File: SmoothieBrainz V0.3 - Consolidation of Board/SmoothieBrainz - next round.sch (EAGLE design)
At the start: 156 parts, among them IC1 LPC1769, IC5 LD117ADT33TR, Q1 BSL207SP, Q2 12MHz, SW1 SW_TACT_4P_B, SW3 SW_TACT_4P_B, U2 HC_05, U3 USD-SOCKETUSD, X1 GMSTBV2, X14 USBPTH, X2 MSTBA2, X3 MSTBA4

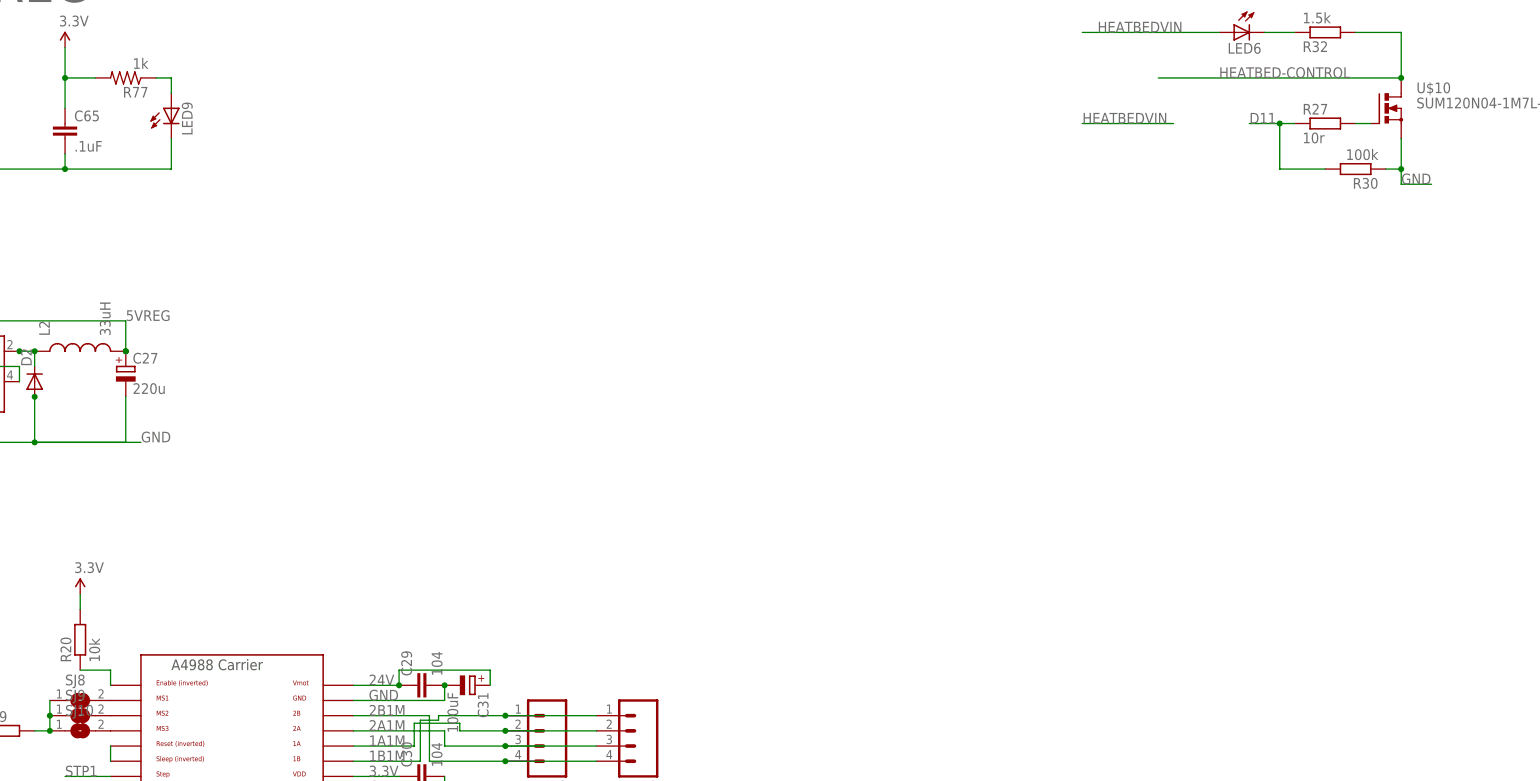
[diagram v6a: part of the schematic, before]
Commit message: lan8720 routed, added mosfets
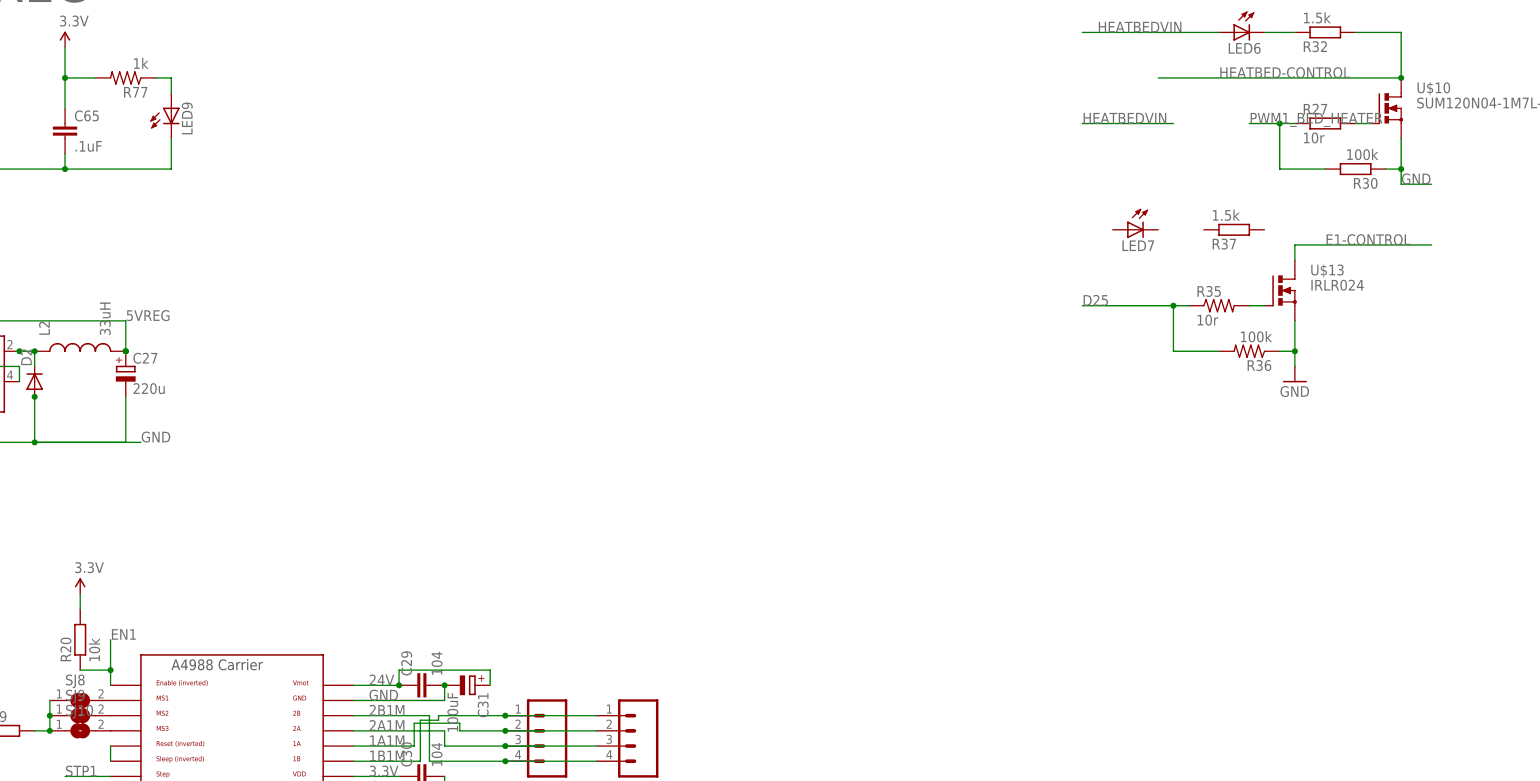
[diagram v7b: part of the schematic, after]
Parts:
- added LED7: (no value), led:LEDSML0805
- added R35: 10r, adafruit:R-US_R0805
- added R36: 100k, adafruit:R-US_R0805
- added R37: 1.5k, resistor:R-EU_R0603
- added U$13: IRLR024, Cohesion_parts:N-POWER-MOSFETDPAK-MOSFET
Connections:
- removed net D11: R27.1, R30.2
- new net D25: R35.1, R36.2
- new net E1-CONTROL: U$13.D
- net EN1: now also R20.1, U$1.EN
- net GND: now also R36.1, U$13.S
- net N$28: now also R35.2, U$13.G; no longer R20.1, U$1.EN
- net PWM1_BED_HEATER: now also R27.1, R30.2
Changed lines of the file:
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@@
 <class number="4" name="30-Amp Class" width="2.54" drill="0">
 </class>
+<class number="5" name="3.3-Amp Class" width="1.27" drill="0">
+</class>
 </classes>
 <parts>
@@
 <part name="U$11" library="adafruit" deviceset="FIDUCIAL" device=""/>
 <part name="U$12" library="adafruit" deviceset="FIDUCIAL" device=""/>
+<part name="U$13" library="Cohesion_parts" deviceset="N-POWER-MOSFET" device="DPAK-MOSFET" value="IRLR024"/>
+<part name="R35" library="adafruit" deviceset="R-US_" device="R0805" value="10r"/>
+<part name="R36" library="adafruit" deviceset="R-US_" device="R0805" value="100k"/>
+<part name="GND15" library="supply1" deviceset="GND" device=""/>
+<part name="LED7" library="led" deviceset="LED" device="SML0805"/>
+<part name="R37" library="resistor" deviceset="R-EU_" device="R0603" value="1.5k"/>
 </parts>
 <sheets>
@@
 <instance part="U$11" gate="G$1" x="17.78" y="215.9"/>
 <instance part="U$12" gate="G$1" x="27.94" y="215.9"/>
+<instance part="U$13" gate="G$1" x="528.32" y="335.28"/>
+<instance part="R35" gate="G$1" x="508" y="332.74"/>
+<instance part="R36" gate="G$1" x="513.08" y="325.12" rot="R180"/>
+<instance part="GND15" gate="1" x="520.7" y="320.04"/>
+<instance part="LED7" gate="G$1" x="492.76" y="345.44" rot="MR270"/>
+<instance part="R37" gate="G$1" x="510.54" y="345.44" rot="MR180"/>
 </instances>
 <busses>
@@
 <label x="78.74" y="281.94" size="1.778" layer="95"/>
 </segment>
+<segment>
+<pinref part="R36" gate="G$1" pin="1"/>
+<pinref part="U$13" gate="G$1" pin="S"/>
+<wire x1="518.16" y1="325.12" x2="520.7" y2="325.12" width="0.1524" layer="91"/>
+<wire x1="520.7" y1="325.12" x2="520.7" y2="330.2" width="0.1524" layer="91"/>
+<pinref part="GND15" gate="1" pin="GND"/>
+<wire x1="520.7" y1="322.58" x2="520.7" y2="325.12" width="0.1524" layer="91"/>
+<junction x="520.7" y="325.12"/>
+</segment>
 </net>
 <net name="3.3V" class="0">
@@
 <wire x1="78.74" y1="398.78" x2="106.68" y2="398.78" width="0.1524" layer="91"/>
 </segment>
+<segment>
+<pinref part="U$1" gate="G$1" pin="EN"/>
+<wire x1="322.58" y1="269.24" x2="322.58" y2="271.78" width="0.1524" layer="91"/>
+<pinref part="R20" gate="G$1" pin="1"/>
+<wire x1="317.5" y1="271.78" x2="322.58" y2="271.78" width="0.1524" layer="91"/>
+<wire x1="322.58" y1="271.78" x2="322.58" y2="276.86" width="0.1524" layer="91"/>
+<junction x="322.58" y="271.78"/>
+<label x="322.58" y="276.86" size="1.778" layer="95"/>
+</segment>
 </net>
 <net name="DIR1" class="0">
@@
 <wire x1="78.74" y1="444.5" x2="106.68" y2="444.5" width="0.1524" layer="91"/>
 </segment>
+<segment>
+<pinref part="R30" gate="G$1" pin="2"/>
+<wire x1="525.78" y1="355.6" x2="518.16" y2="355.6" width="0.1524" layer="91"/>
+<wire x1="518.16" y1="355.6" x2="518.16" y2="363.22" width="0.1524" layer="91"/>
+<pinref part="R27" gate="G$1" pin="1"/>
+<wire x1="518.16" y1="363.22" x2="520.7" y2="363.22" width="0.1524" layer="91"/>
+<wire x1="518.16" y1="363.22" x2="513.08" y2="363.22" width="0.1524" layer="91"/>
+<junction x="518.16" y="363.22"/>
+<label x="513.08" y="363.22" size="1.778" layer="95"/>
+</segment>
 </net>
 <net name="Y_MIN" class="0">
@@
 </segment>
 </net>
-<net name="D11" class="0">
-<segment>
-<pinref part="R30" gate="G$1" pin="2"/>
-<wire x1="525.78" y1="355.6" x2="518.16" y2="355.6" width="0.1524" layer="91"/>
-<wire x1="518.16" y1="355.6" x2="518.16" y2="363.22" width="0.1524" layer="91"/>
-<pinref part="R27" gate="G$1" pin="1"/>
-<wire x1="518.16" y1="363.22" x2="520.7" y2="363.22" width="0.1524" layer="91"/>
-<wire x1="518.16" y1="363.22" x2="513.08" y2="363.22" width="0.1524" layer="91"/>
-<junction x="518.16" y="363.22"/>
-<label x="513.08" y="363.22" size="1.778" layer="95"/>
-</segment>
-</net>
 <net name="HEATBED-CONTROL" class="0">
 <segment>
@@
 </segment>
 </net>
+<net name="D25" class="0">
+<segment>
+<pinref part="R35" gate="G$1" pin="1"/>
+<wire x1="502.92" y1="332.74" x2="500.38" y2="332.74" width="0.1524" layer="91"/>
+<pinref part="R36" gate="G$1" pin="2"/>
+<wire x1="500.38" y1="332.74" x2="485.14" y2="332.74" width="0.1524" layer="91"/>
+<wire x1="508" y1="325.12" x2="500.38" y2="325.12" width="0.1524" layer="91"/>
+<wire x1="500.38" y1="325.12" x2="500.38" y2="332.74" width="0.1524" layer="91"/>
+<junction x="500.38" y="332.74"/>
+<label x="485.14" y="332.74" size="1.778" layer="95"/>
+</segment>
+</net>
+<net name="E1-CONTROL" class="5">
+<segment>
+<pinref part="U$13" gate="G$1" pin="D"/>
+<wire x1="520.7" y1="340.36" x2="520.7" y2="342.9" width="0.1524" layer="91"/>
+<wire x1="520.7" y1="342.9" x2="543.56" y2="342.9" width="0.1524" layer="91"/>
+<label x="525.78" y="342.9" size="1.778" layer="95"/>
+</segment>
+</net>
 <net name="N$28" class="0">
 <segment>
-<pinref part="U$1" gate="G$1" pin="EN"/>
-<wire x1="322.58" y1="269.24" x2="322.58" y2="271.78" width="0.1524" layer="91"/>
-<pinref part="R20" gate="G$1" pin="1"/>
-<wire x1="317.5" y1="271.78" x2="322.58" y2="271.78" width="0.1524" layer="91"/>
+<pinref part="R35" gate="G$1" pin="2"/>
+<pinref part="U$13" gate="G$1" pin="G"/>
+<wire x1="513.08" y1="332.74" x2="515.62" y2="332.74" width="0.1524" layer="91"/>
 </segment>
 </net>
